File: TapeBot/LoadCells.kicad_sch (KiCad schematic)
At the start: 36 parts, among them J1 43045-0412, J2 43045-0412, Q1 MMBT4403, Q2 MMBT4403, U2 HX711, U3 HX711

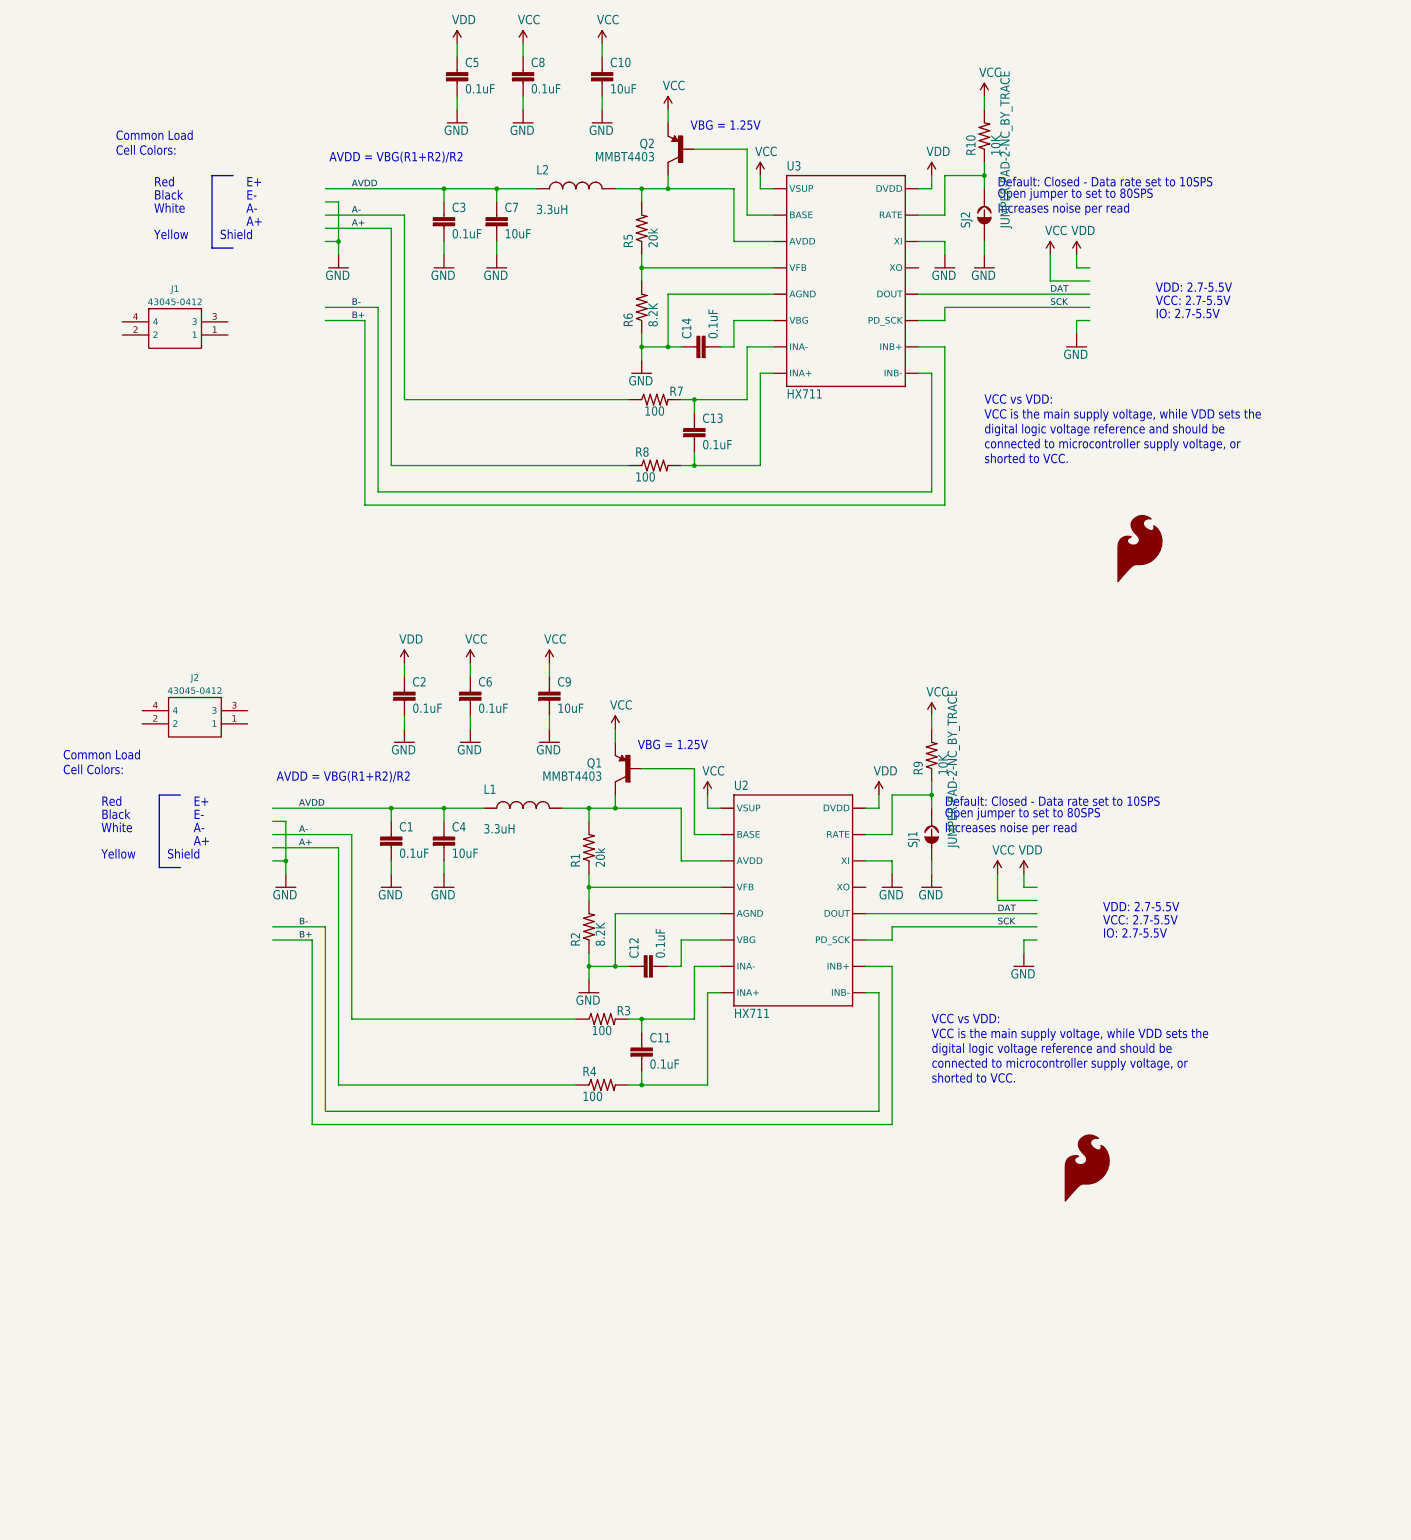
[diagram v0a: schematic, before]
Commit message: fixed footprints and symbols
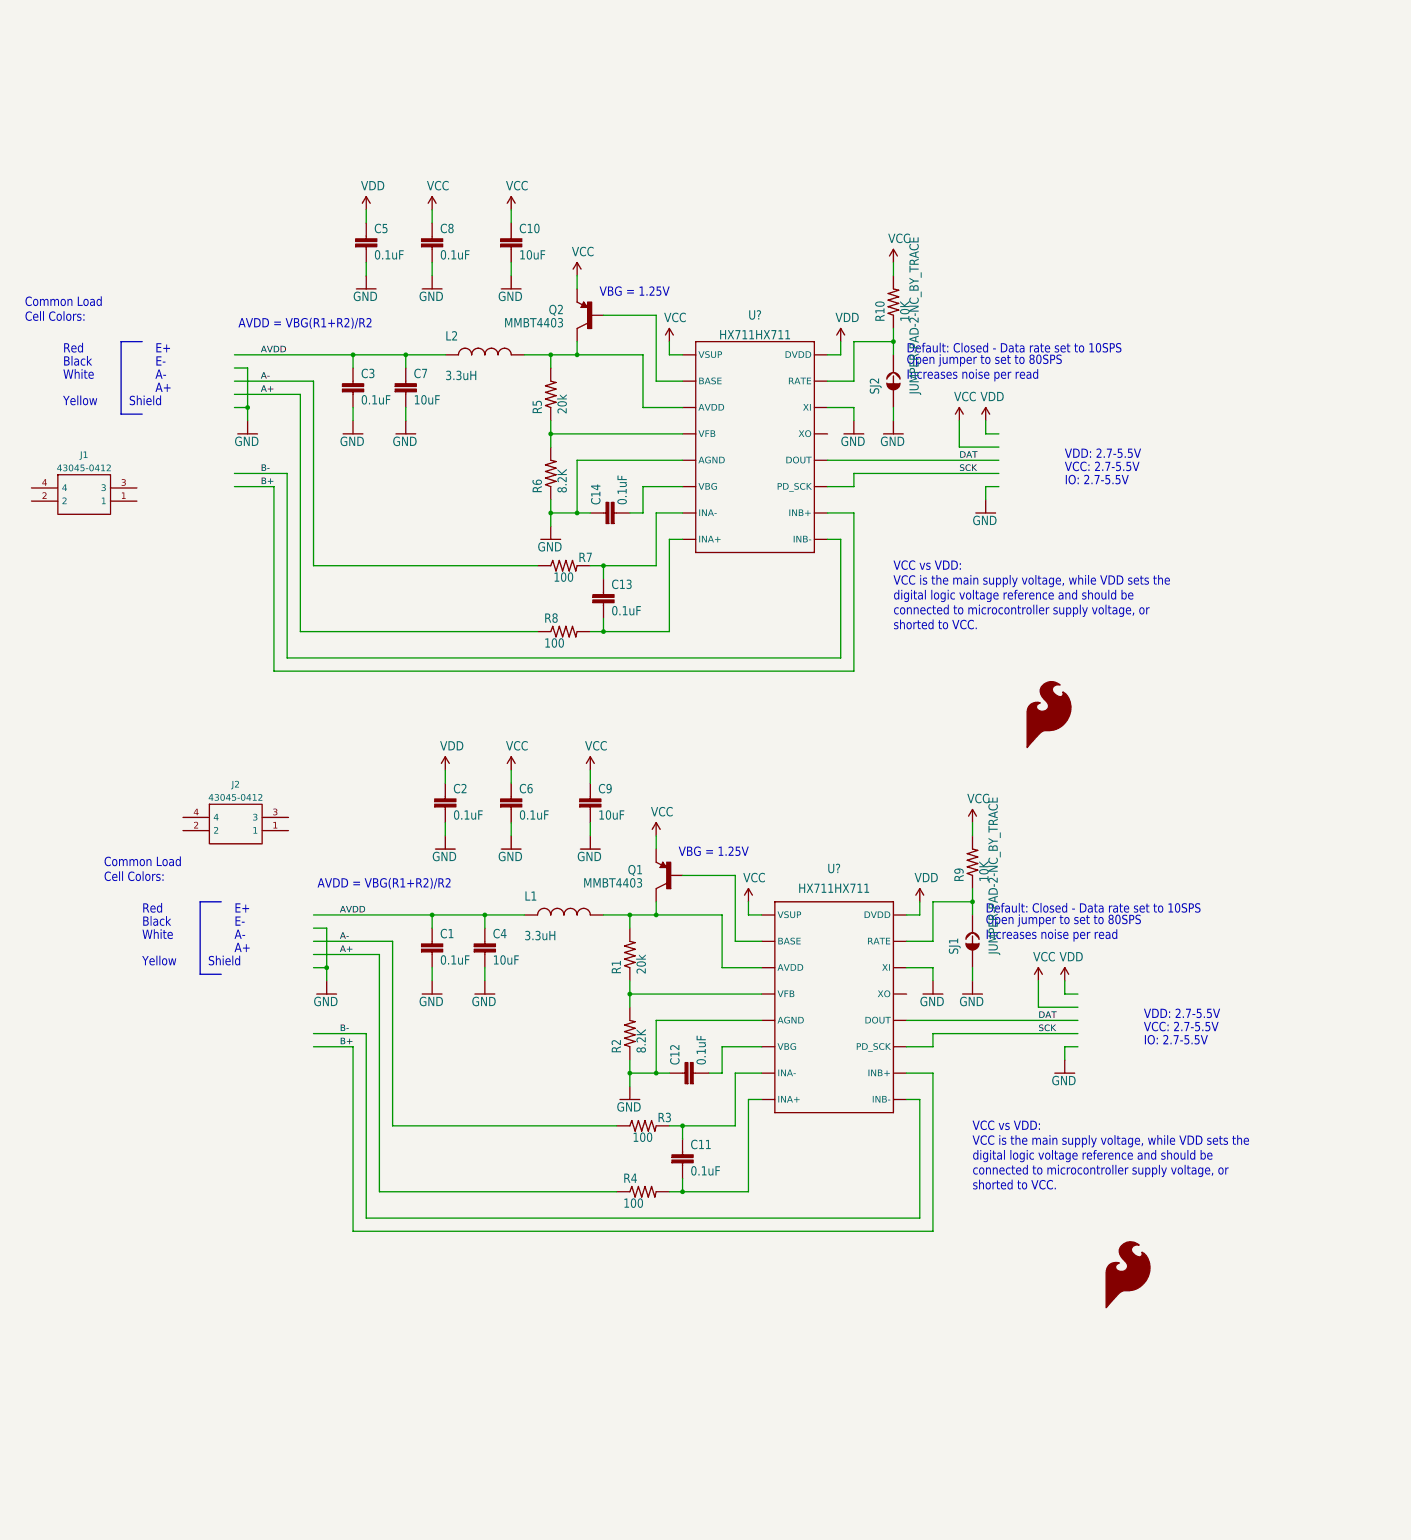
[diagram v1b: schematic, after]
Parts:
- removed U2, U3: HX711, SparkFun_HX711_Load_Cell:SO16, symbol SparkFun_HX711_Load_Cell-eagle-import:HX711HX711
- added U? (x2): HX711HX711, tapebot:SOP127P600X180-16N, symbol tapebot:HX711HX711
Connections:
- net B+: now also U?.10 (INB+), U?.10 (INB+)
- net B-: now also U?.9 (INB-), U?.9 (INB-)
- net DAT: now also U?.12 (DOUT), U?.12 (DOUT)
- net GND: now also U?.14 (XI), U?.14 (XI), U?.5 (AGND), U?.5 (AGND)
- net SCK: now also U?.11 (PD_SCK), U?.11 (PD_SCK)
- net VCC: now also U?.1 (VSUP), U?.1 (VSUP)
- net VDD: now also U?.16 (DVDD), U?.16 (DVDD)
- net at C13.2, R8.2: now also U?.8 (INA+)
- net at R9.1, SJ1.2: now also U?.15 (RATE)
- net at C13.1, R7.2: now also U?.7 (INA-)
- net at R10.1, SJ2.2: now also U?.15 (RATE)
- net at C12.2: now also U?.6 (VBG)
- net at L1.2, Q1.3 (C), R1.2: now also U?.3 (AVDD)
- net at R1.1, R2.2: now also U?.4 (VFB)
- net at C11.1, R3.2: now also U?.7 (INA-)
- net at C11.2, R4.2: now also U?.8 (INA+)
- net at R5.1, R6.2: now also U?.4 (VFB)
- net at L2.2, Q2.3 (C), R5.2: now also U?.3 (AVDD)
- net at Q2.1 (B): now also U?.2 (BASE)
- net at Q1.1 (B): now also U?.2 (BASE)
- net at C14.2: now also U?.6 (VBG)
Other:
- moved on the sheet: C1, C10, C11, C12, C13, C14, C2, C3, C4, C5, C6, C7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

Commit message: finished motor driver schematic and load cell schematic
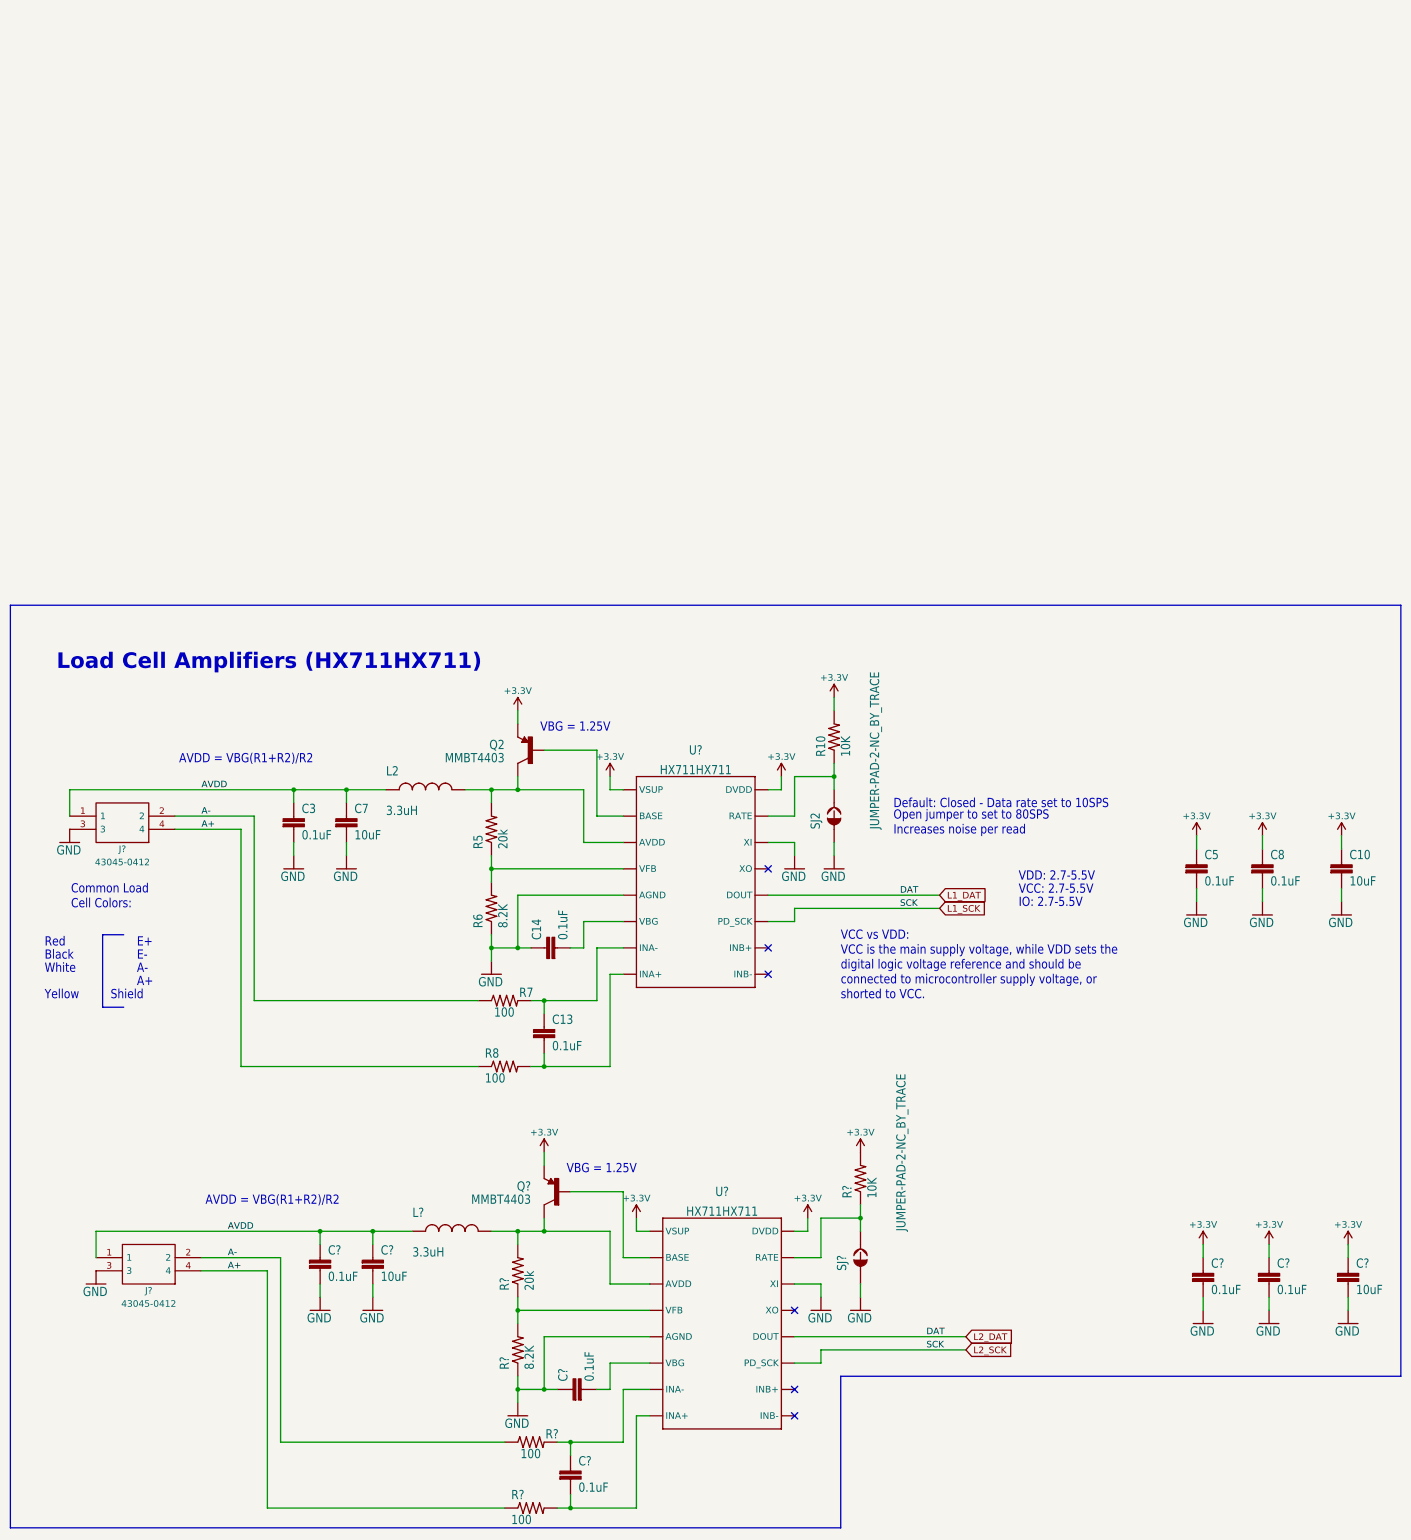
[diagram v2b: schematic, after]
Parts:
- removed C1, C11, C12, C2, C6: 0.1uF, SparkFun_HX711_Load_Cell:0603-CAP, symbol SparkFun_HX711_Load_Cell-eagle-import:0.1UF-25V-5%(0603)
- removed C4, C9: 10uF, SparkFun_HX711_Load_Cell:1210, symbol SparkFun_HX711_Load_Cell-eagle-import:10UF50V20%(1210)
- removed J1, J2: 43045-0412, 43045-04(12,13,14), symbol tapebot:43045-0412
- removed L1: 3.3uH, SparkFun_HX711_Load_Cell:0805, symbol SparkFun_HX711_Load_Cell-eagle-import:INDUCTOR0805-IND
- removed LOGO1, LOGO2: SFE_LOGO_FLAME.1_INCH, SparkFun_HX711_Load_Cell:SFE_LOGO_FLAME_.1, symbol SparkFun_HX711_Load_Cell-eagle-import:SFE_LOGO_FLAME.1_INCH
- removed Q1: MMBT4403, SparkFun_HX711_Load_Cell:SOT23-3, symbol SparkFun_HX711_Load_Cell-eagle-import:TRANSISTOR_PNPMMBT4403
- removed R1: 20k, SparkFun_HX711_Load_Cell:0603-RES, symbol SparkFun_HX711_Load_Cell-eagle-import:20KOHM1/10W1%(0603)
- removed R2: 8.2K, SparkFun_HX711_Load_Cell:0603-RES, symbol SparkFun_HX711_Load_Cell-eagle-import:8.2KOHM-1/10W-5%(0603)
- removed R3, R4: 100, SparkFun_HX711_Load_Cell:0603-RES, symbol SparkFun_HX711_Load_Cell-eagle-import:100OHM-1/10W-1%(0603)
- removed R9: 10K, SparkFun_HX711_Load_Cell:0603-RES, symbol SparkFun_HX711_Load_Cell-eagle-import:10KOHM-1/10W-1%(0603)0603
- removed SJ1: JUMPER-PAD-2-NC_BY_TRACE, SparkFun_HX711_Load_Cell:PAD-JUMPER-2-NC_BY_TRACE_YES_SILK, symbol SparkFun_HX711_Load_Cell-eagle-import:JUMPER-PAD-2-NC_BY_TRACE
- removed U?: HX711HX711, tapebot:SOP127P600X180-16N, symbol tapebot:HX711HX711
- added C? (x2): 10uF, SparkFun_HX711_Load_Cell:1210, symbol SparkFun_HX711_Load_Cell-eagle-import:10UF50V20%(1210)
- added C? (x5): 0.1uF, SparkFun_HX711_Load_Cell:0603-CAP, symbol SparkFun_HX711_Load_Cell-eagle-import:0.1UF-25V-5%(0603)
- added J? (x2): 43045-0412, tapebot:43045-04YY_121314, symbol tapebot:43045-0412
- added L?: 3.3uH, SparkFun_HX711_Load_Cell:0805, symbol SparkFun_HX711_Load_Cell-eagle-import:INDUCTOR0805-IND
- added Q?: MMBT4403, SparkFun_HX711_Load_Cell:SOT23-3, symbol SparkFun_HX711_Load_Cell-eagle-import:TRANSISTOR_PNPMMBT4403
- added R?: 20k, SparkFun_HX711_Load_Cell:0603-RES, symbol SparkFun_HX711_Load_Cell-eagle-import:20KOHM1/10W1%(0603)
- added R?: 10K, SparkFun_HX711_Load_Cell:0603-RES, symbol SparkFun_HX711_Load_Cell-eagle-import:10KOHM-1/10W-1%(0603)0603
- added R?: 8.2K, SparkFun_HX711_Load_Cell:0603-RES, symbol SparkFun_HX711_Load_Cell-eagle-import:8.2KOHM-1/10W-5%(0603)
- added R? (x2): 100, SparkFun_HX711_Load_Cell:0603-RES, symbol SparkFun_HX711_Load_Cell-eagle-import:100OHM-1/10W-1%(0603)
- added SJ?: JUMPER-PAD-2-NC_BY_TRACE, SparkFun_HX711_Load_Cell:PAD-JUMPER-2-NC_BY_TRACE_YES_SILK, symbol SparkFun_HX711_Load_Cell-eagle-import:JUMPER-PAD-2-NC_BY_TRACE
- added U?: HX711HX711, tapebot:SOP127P600X180-16N, symbol tapebot:HX711HX711
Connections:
- net VDD is gone; now on net +3.3V: C5.1, U?.16 (DVDD)
- net A+: now also J?.4, J?.4, R?.1
- net A-: now also J?.2, J?.2, R?.1
- net AVDD: now also C?.1, C?.1, J?.1, J?.1, L?.1
- net GND: now also C?.1, C?.2, C?.2, C?.2, C?.2, C?.2, J?.3, J?.3, R?.1, SJ?.1, U?.14 (XI), U?.5 (AGND)
- net B+: no longer names the net of U?.10 (INB+)
- net B-: no longer names the net of U?.9 (INB-)
- net DAT renamed L1_DAT
- net L1_DAT: now also U?.12 (DOUT)
- net SCK renamed L1_SCK
- net L1_SCK: now also U?.11 (PD_SCK)
- net VCC renamed +3.3V
- net +3.3V: now also C?.1, C?.1, C?.1, Q?.2 (E), R?.2, U?.1 (VSUP), U?.16 (DVDD)
- new net: L?.2, Q?.3 (C), R?.2, U?.3 (AVDD)
- new net: C?.2, U?.6 (VBG)
- new net: R?.1, R?.2, U?.4 (VFB)
- new net: C?.1, R?.2, U?.7 (INA-)
- new net: C?.2, R?.2, U?.8 (INA+)
- new net: R?.1, SJ?.2, U?.15 (RATE)
- new net: Q?.1 (B), U?.2 (BASE)
- no-connect marks 0 -> 6
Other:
- note added: "Load Cell Amplifiers (HX711HX711)"
- moved on the sheet: C10, C13, C14, C3, C5, C7, C8, L2, Q2, R10, R5, R6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

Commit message: (mostly) finished schematic
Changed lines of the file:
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@@
-    (stroke (width 0) (type default) (color 0 0 0 0))
-  )
-  (polyline (pts (xy 13.97 193.04) (xy 173.99 193.04))
     (stroke (width 0) (type default) (color 0 0 0 0))
   )
@@
     (stroke (width 0) (type default) (color 0 0 0 0))
   )
-  (polyline (pts (xy 281.94 163.83) (xy 281.94 15.24))
-    (stroke (width 0) (type default) (color 0 0 0 0))
-  )
   (wire (pts (xy 111.76 48.26) (xy 111.76 50.8))
     (stroke (width 0) (type default) (color 0 0 0 0))
@@
     (stroke (width 0) (type default) (color 0 0 0 0))
   )
-  (polyline (pts (xy 13.97 15.24) (xy 281.94 15.24))
-    (stroke (width 0) (type default) (color 0 0 0 0))
-  )
   (wire (pts (xy 129.54 146.05) (xy 129.54 135.89))
     (stroke (width 0) (type default) (color 0 0 0 0))
@@
     (stroke (width 0) (type default) (color 0 0 0 0))
   )
-  (polyline (pts (xy 13.97 15.24) (xy 13.97 193.04))
-    (stroke (width 0) (type default) (color 0 0 0 0))
-  )
   (wire (pts (xy 101.6 50.8) (xy 106.68 50.8))
     (stroke (width 0) (type default) (color 0 0 0 0))
@@
     (stroke (width 0) (type default) (color 0 0 0 0))
   )
-  (polyline (pts (xy 173.99 193.04) (xy 173.99 163.83))
-    (stroke (width 0) (type default) (color 0 0 0 0))
-  )
   (wire (pts (xy 177.8 133.35) (xy 170.18 133.35))
     (stroke (width 0) (type default) (color 0 0 0 0))
@@
     (stroke (width 0) (type default) (color 0 0 0 0))
   )
-  (polyline (pts (xy 173.99 163.83) (xy 281.94 163.83))
-    (stroke (width 0) (type default) (color 0 0 0 0))
-  )
